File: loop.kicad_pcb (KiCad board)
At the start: 2 copper layers, 38 x 38 mm, 12 parts, among them Q1 BSS138, SW1 SW_Push, U1 CD4013

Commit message: Add series r
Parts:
- removed C3: 100n, Capacitor_SMD:C_0805_2012Metric_Pad1.18x1.45mm_HandSolder
- added C4: 22u, Capacitor_SMD:C_0805_2012Metric_Pad1.18x1.45mm_HandSolder, B.Cu at (113.4, 59.2)
- added C5: 10u, Capacitor_SMD:C_0805_2012Metric_Pad1.18x1.45mm_HandSolder, B.Cu at (123.2, 59.2)
- added R5: 1k, Resistor_SMD:R_0805_2012Metric_Pad1.20x1.40mm_HandSolder, B.Cu at (118.3, 59.2)
- added R6: 33, Resistor_SMD:R_0805_2012Metric_Pad1.20x1.40mm_HandSolder, F.Cu at (130.4, 55.0)
- moved D1 0.50 mm to (118.3, 48.0)
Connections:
- D1 pad 2: +3V0 -> Net-(D1-A)
- U1 pad 14: +3V0 -> V_F
- U1 pad 4: +3V0 -> V_F
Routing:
- net Net-(D1-A): track 0.00 -> 14.4 mm
- net V_F: track 0.00 -> 14.2 mm
- net +3V0: track 70.1 -> 56.6 mm
- net GATE: track 10.6 -> 12.4 mm
- net GND: vias 7 -> 5

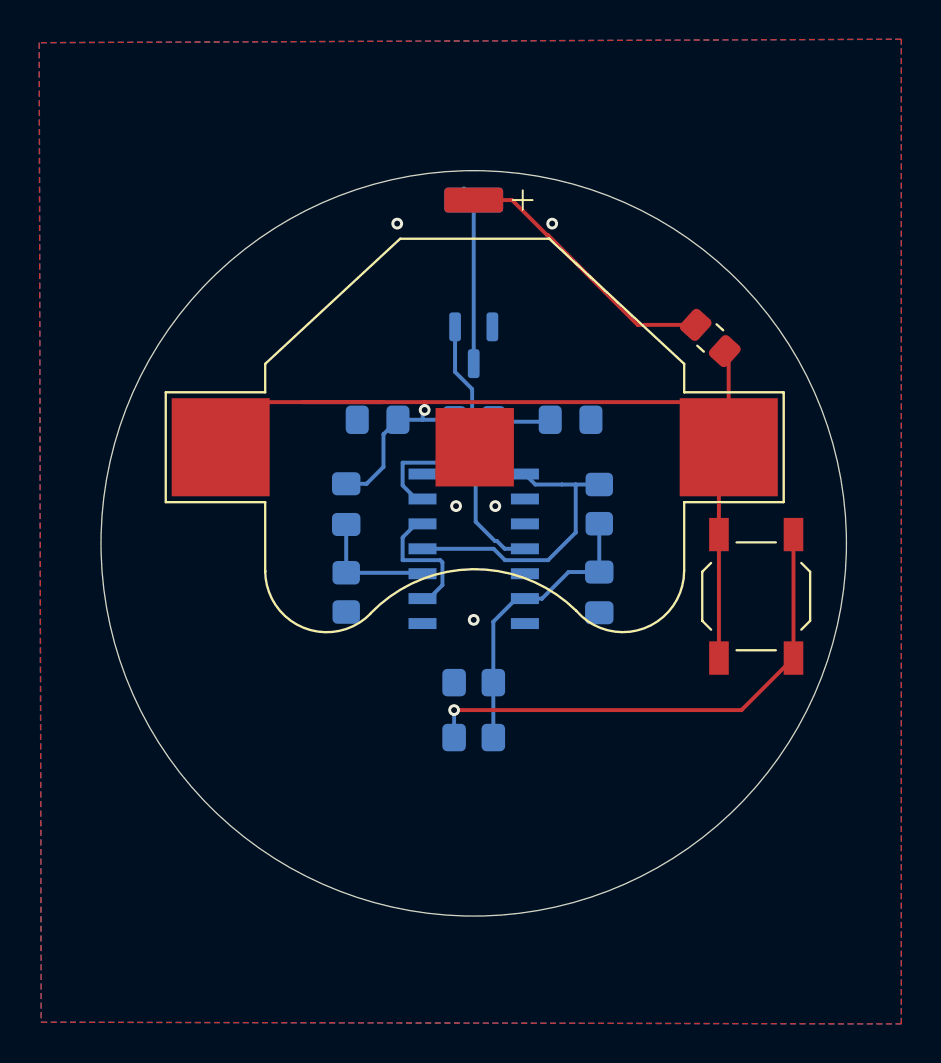
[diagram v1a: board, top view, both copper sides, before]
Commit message: Add part nr and edge hole
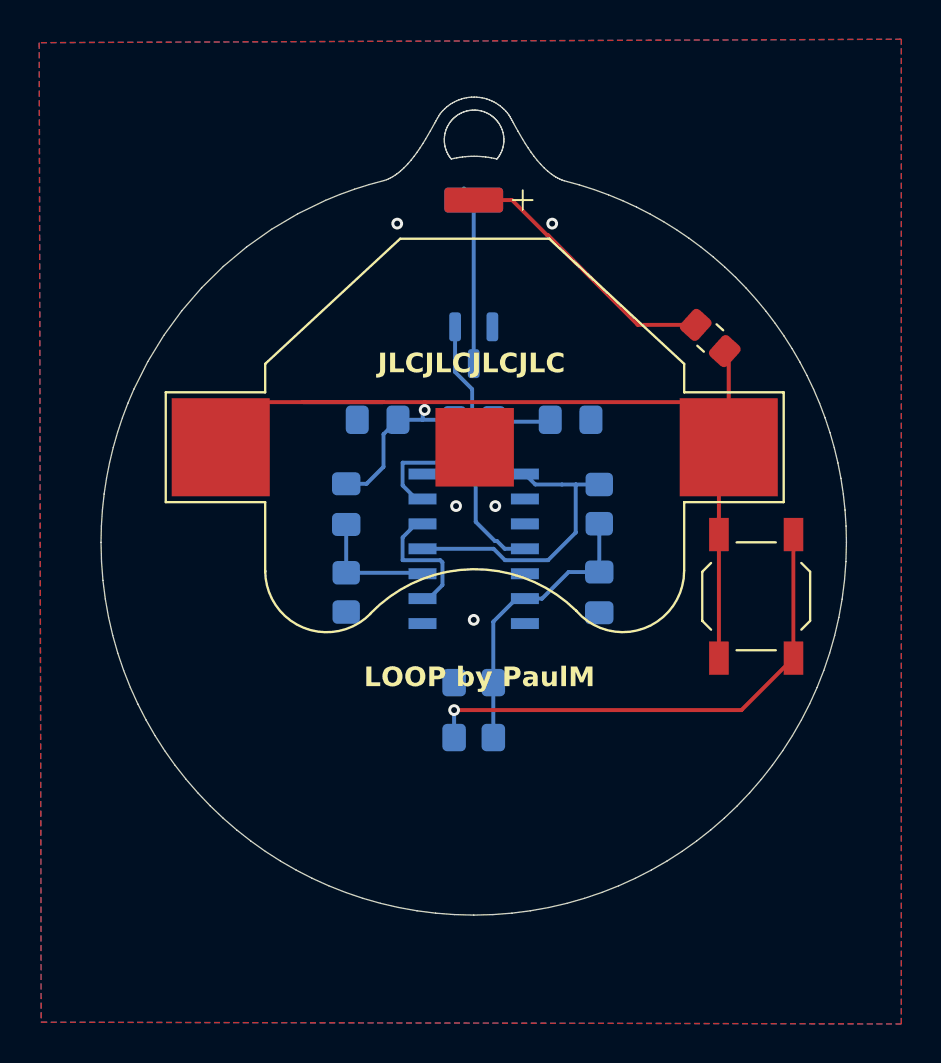
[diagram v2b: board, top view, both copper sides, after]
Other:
- board size 38 x 38 mm -> 38 x 41.7 mm
- board text added: "JLCJLCJLCJLC"
- board text added: "LOOP by PaulM"

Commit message: Add exposed copper
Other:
- board text removed: "JLCJLCJLCJLC"
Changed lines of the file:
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@@
+	(gr_poly
+		(pts
+			(xy 122.510732 50.410026) (xy 123.138887 50.600221) (xy 123.755565 50.81592) (xy 124.360148 51.056503)
+			(xy 124.952018 51.321353) (xy 125.530555 51.609851) (xy 126.095142 51.92138) (xy 126.645161 52.255321)
+			(xy 127.179993 52.611056) (xy 127.69902 52.987967) (xy 128.201625 53.385435) (xy 128.687188 53.802843)
+			(xy 129.155091 54.239573) (xy 129.604717 54.695005) (xy 130.035447 55.168523) (xy 130.446662 55.659507)
+			(xy 130.837746 56.16734) (xy 131.208078 56.691403) (xy 131.557042 57.231078) (xy 131.884018 57.785748)
+			(xy 132.188389 58.354793) (xy 132.469537 58.937596) (xy 132.726842 59.533539) (xy 132.959688 60.142003)
+			(xy 133.167455 60.76237) (xy 133.349526 61.394021) (xy 133.505282 62.03634) (xy 133.634105 62.688708)
+			(xy 133.735377 63.350505) (xy 133.80848 64.021115) (xy 133.852795 64.699919) (xy 133.867704 65.386299)
+			(xy 133.847456 66.185934) (xy 133.787366 66.975128) (xy 133.688414 67.752901) (xy 133.551579 68.518273)
+			(xy 133.377843 69.270265) (xy 133.168184 70.007895) (xy 132.923583 70.730185) (xy 132.64502 71.436153)
+			(xy 132.333476 72.124821) (xy 131.989929 72.795207) (xy 131.615361 73.446332) (xy 131.210751 74.077216)
+			(xy 130.777079 74.686879) (xy 130.315326 75.27434) (xy 129.826471 75.83862) (xy 129.311494 76.378738)
+			(xy 128.771376 76.893715) (xy 128.207097 77.382571) (xy 127.619636 77.844325) (xy 127.009973 78.277997)
+			(xy 126.37909 78.682607) (xy 125.727965 79.057176) (xy 125.057579 79.400722) (xy 124.368912 79.712267)
+			(xy 123.662943 79.99083) (xy 122.940654 80.235431) (xy 122.203024 80.44509) (xy 121.451032 80.618827)
+			(xy 120.68566 80.755661) (xy 119.907887 80.854614) (xy 119.118693 80.914704) (xy 118.319059 80.934952)
+			(xy 117.519424 80.914704) (xy 116.730229 80.854614) (xy 115.952456 80.755661) (xy 115.187083 80.618827)
+			(xy 114.435091 80.44509) (xy 113.69746 80.235431) (xy 112.97517 79.99083) (xy 112.269202 79.712267)
+			(xy 111.580534 79.400722) (xy 110.910148 79.057176) (xy 110.259022 78.682607) (xy 109.628139 78.277997)
+			(xy 109.018476 77.844325) (xy 108.431015 77.382571) (xy 107.866735 76.893715) (xy 107.326617 76.378738)
+			(xy 106.81164 75.83862) (xy 106.322785 75.27434) (xy 105.861031 74.686879) (xy 105.427359 74.077216)
+			(xy 105.022749 73.446332) (xy 104.648181 72.795207) (xy 104.304634 72.124821) (xy 103.99309 71.436153)
+			(xy 103.714527 70.730185) (xy 103.469926 70.007895) (xy 103.260268 69.270265) (xy 103.086531 68.518273)
+			(xy 102.949696 67.752901) (xy 102.850744 66.975128) (xy 102.790654 66.185934) (xy 102.770406 65.386299)
+			(xy 102.785255 64.701297) (xy 102.829391 64.023839) (xy 102.9022 63.354539) (xy 103.003069 62.694012)
+			(xy 103.131381 62.042872) (xy 103.286524 61.401733) (xy 103.467883 60.77121) (xy 103.674843 60.151918)
+			(xy 103.90679 59.544471) (xy 104.16311 58.949483) (xy 104.74641 57.799343) (xy 105.419829 56.706415)
+			(xy 106.178452 55.675614) (xy 107.017363 54.711856) (xy 107.931649 53.820056) (xy 108.916393 53.00513)
+			(xy 109.966682 52.271994) (xy 111.0776 51.625564) (xy 112.244232 51.070755) (xy 112.846905 50.829245)
+			(xy 113.461664 50.612484) (xy 114.087894 50.421085) (xy 114.724981 50.255665) (xy 114.724981 53.650032)
+			(xy 114.258254 53.803345) (xy 113.799949 53.974622) (xy 113.350486 54.163445) (xy 112.910283 54.369393)
+			(xy 112.47976 54.592047) (xy 112.059336 54.830988) (xy 111.649431 55.085797) (xy 111.250464 55.356054)
+			(xy 110.862854 55.64134) (xy 110.487022 55.941235) (xy 110.123385 56.25532) (xy 109.772364 56.583176)
+			(xy 109.434378 56.924384) (xy 109.109846 57.278523) (xy 108.799188 57.645174) (xy 108.502823 58.023919)
+			(xy 108.221171 58.414338) (xy 107.95465 58.816011) (xy 107.703681 59.228519) (xy 107.468681 59.651443)
+			(xy 107.250072 60.084363) (xy 107.048273 60.52686) (xy 106.863701 60.978515) (xy 106.696778 61.438907)
+			(xy 106.547923 61.907619) (xy 106.417554 62.38423) (xy 106.306091 62.868321) (xy 106.213954 63.359473)
+			(xy 106.141562 63.857266) (xy 106.089334 64.361281) (xy 106.057689 64.871099) (xy 106.047048 65.386299)
+			(xy 106.063029 66.017408) (xy 106.110458 66.640279) (xy 106.18856 67.254137) (xy 106.296561 67.858209)
+			(xy 106.433689 68.451722) (xy 106.59917 69.033901) (xy 106.792229 69.603974) (xy 107.012094 70.161167)
+			(xy 107.257991 70.704705) (xy 107.529145 71.233816) (xy 107.824785 71.747726) (xy 108.144135 72.245662)
+			(xy 108.486422 72.726848) (xy 108.850873 73.190513) (xy 109.236714 73.635883) (xy 109.643172 74.062183)
+			(xy 110.069472 74.46864) (xy 110.514842 74.85448) (xy 110.978507 75.218931) (xy 111.459694 75.561218)
+			(xy 111.95763 75.880568) (xy 112.47154 76.176207) (xy 113.000651 76.447361) (xy 113.54419 76.693258)
+			(xy 114.101383 76.913122) (xy 114.671456 77.106181) (xy 115.253636 77.271662) (xy 115.847149 77.408789)
+			(xy 116.451221 77.516791) (xy 117.065079 77.594893) (xy 117.68795 77.642321) (xy 118.319059 77.658302)
+			(xy 118.950167 77.642321) (xy 119.573037 77.594893) (xy 120.186894 77.516791) (xy 120.790966 77.408789)
+			(xy 121.384478 77.271662) (xy 121.966657 77.106181) (xy 122.536729 76.913122) (xy 123.093921 76.693258)
+			(xy 123.637459 76.447361) (xy 124.166569 76.176207) (xy 124.680478 75.880568) (xy 125.178413 75.561218)
+			(xy 125.659599 75.218931) (xy 126.123264 74.85448) (xy 126.568632 74.46864) (xy 126.994932 74.062183)
+			(xy 127.401388 73.635883) (xy 127.787229 73.190513) (xy 128.151679 72.726848) (xy 128.493965 72.245662)
+			(xy 128.813315 71.747726) (xy 129.108953 71.233816) (xy 129.380107 70.704705) (xy 129.626003 70.161167)
+			(xy 129.845868 69.603974) (xy 130.038926 69.033901) (xy 130.204407 68.451722) (xy 130.341534 67.858209)
+			(xy 130.449535 67.254137) (xy 130.527637 66.640279) (xy 130.575065 66.017408) (xy 130.591047 65.386299)
+			(xy 130.580347 64.869693) (xy 130.548528 64.3585) (xy 130.496015 63.853143) (xy 130.423229 63.354045)
+			(xy 130.330593 62.861629) (xy 130.218531 62.376318) (xy 129.937819 61.428701) (xy 129.584476 60.514577)
+			(xy 129.161885 59.637329) (xy 128.673431 58.800339) (xy 128.122495 58.006989) (xy 127.512462 57.260663)
+			(xy 126.846716 56.564742) (xy 126.128639 55.92261) (xy 125.361615 55.337649) (xy 124.549027 54.813242)
+			(xy 123.694259 54.352771) (xy 122.800695 53.959619) (xy 121.871717 53.637169) (xy 121.871717 50.245953)
+		)
+		(stroke
+			(width 0.131431)
+			(type solid)
+		)
+		(fill yes)
+		(layer "B.Mask")
+	)
 	(gr_poly
 		(pts
@@
 		)
 	)
-	(gr_text "JLCJLCJLCJLC"
-		(at 113.4 56.9 0)
-		(layer "F.SilkS")
-		(effects
-			(font
-				(size 1 1)
-				(bold yes)
-			)
-			(justify left bottom)
-		)
-	)
 	(segment
 		(start 109.6 58.3)
@@
 	)
 	(group ""
+		(members "41ba2b42-e2d7-43cf-b143-63aa0d0c4f92")
+	)
+	(group ""

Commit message: Note about bug
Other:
- board text added: "Pin 1 and 2 on U1 are swapped in part from lcsc, fix in post"
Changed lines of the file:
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@@
+		)
+	)
+	(gr_text "Pin 1 and 2 on U1 are swapped in part from lcsc, fix in post"
+		(at 100.9 35.9 0)
+		(layer "F.Fab")
+		(effects
+			(font
+				(size 1 1)
+				(thickness 0.15)
+			)
+			(justify left bottom)
 		)
 	)

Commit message: Update PCB
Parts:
- removed C5: 10u, Capacitor_SMD:C_0805_2012Metric_Pad1.18x1.45mm_HandSolder
- removed the R4 at (124.7, 63.5)
- removed R5: 1k, Resistor_SMD:R_0805_2012Metric_Pad1.20x1.40mm_HandSolder
- added J1: Conn_01x03_Socket, Connector_PinSocket_2.54mm:PinSocket_1x03_P2.54mm_Vertical, F.Cu at (135.5, 68.0)
- BT1: footprint Battery:BatteryHolder_Multicomp_BC-2001_1x2032 -> easyeda2kicad:BAT-SMD_MY-1220-03
- C2: value 100n -> 10u; moved to F.Cu
- C3: renamed from C4; moved to F.Cu
- R1: value 100k -> 1k
- R2: value 100k -> 1M
- R3: value 1M -> 470; moved to F.Cu
- U1: value CD4013 -> ATtiny202-SS; footprint LCSC:SOP-14_L8.7-W3.9-P1.27-LS6.0-BL -> Package_SO:SOIC-8_3.9x4.9mm_P1.27mm
- moved SW1 20.7 mm to (118.5, 53.2)
- moved C2 17.0 mm to (111.7, 57.1), turned to 45 degrees
- moved R2 11.3 mm to (123.4, 65.3), turned to -90 degrees
- moved C3 10.4 mm to (109.2, 68.7)
- moved R3 9.90 mm to (127.4, 68.7), turned to 180 degrees
- moved C1 9.01 mm to (118.3, 69.7), turned to 0 degrees
- moved R4 5.77 mm to (125.1, 57.4), turned to 135 degrees
- moved Q1 3.94 mm to (118.3, 59.3)
- moved BT1 3.90 mm to (118.3, 64.5)
- moved R1 3.04 mm to (113.2, 65.3)
- moved U1 0.48 mm to (118.3, 65.3), turned to 0 degrees
- renumbered R6 to R4
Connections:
- C1 pad 2: Net-(U1-2CD) -> GND
- C2 pad 1: Net-(U1-1SD) -> +3V0
- R1 pad 1: Net-(U1-2CD) -> Net-(R1-Pad1)
- R1 pad 2: GND -> Net-(U1-PA2)
- R2 pad 1: Net-(R2-Pad1) -> GND
- R2 pad 2: Net-(U1-1SD) -> GATE
- R3 pad 1: GND -> UPDI
- R3 pad 2: Net-(U1-1SD) -> Net-(U1-~{RESET}/PA0)
- SW1 pad 1: +3V0 -> Net-(R1-Pad1)
- SW1 pad 2: Net-(R2-Pad1) -> GND
- U1 pad 1: Net-(U1-1Q) -> +3V0
- U1 pad 3: GND -> unconnected-(U1-PA7-Pad3)
- U1 pad 4: V_F -> unconnected-(U1-PA1-Pad4)
- U1 pad 5: GND -> Net-(U1-PA2)
- U1 pad 6: Net-(U1-1SD) -> Net-(U1-~{RESET}/PA0)
- U1 pad 7: GND -> GATE
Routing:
- net Net-(R2-Pad1): track 26.1 -> 0.00 mm, vias 1 -> 0
- net Net-(R1-Pad1): track 0.00 -> 17.9 mm, vias 0 -> 1
- net Net-(U1-1Q): track 15.1 -> 0.00 mm
- net Net-(U1-1SD): track 14.8 -> 0.00 mm
- net V_F: track 14.2 -> 0.00 mm
- net Net-(U1-~{RESET}/PA0): track 0.00 -> 11.6 mm, vias 0 -> 1
- net Net-(U1-PA2): track 0.00 -> 8.97 mm
- net UPDI: track 0.00 -> 7.39 mm
- net +3V0: track 56.6 -> 49.5 mm
- net Net-(U1-2D): track 7.00 -> 0.00 mm
- net Net-(U1-2CD): track 6.37 -> 0.00 mm
- net GND: track 0.00 -> 6.30 mm, vias 5 -> 2
- net Net-(D1-K): track 9.14 -> 12.3 mm
- net Net-(D1-A): track 14.4 -> 13.3 mm
- net GATE: track 12.4 -> 13.6 mm
